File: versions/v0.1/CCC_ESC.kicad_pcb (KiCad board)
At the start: 4 copper layers, 100 x 65 mm, 160 parts, among them J1 Conn_01x04, J2 Conn_01x04, J3 Conn_01x06, J4 Conn_01x06, U1 NCP5183, U2 NCP5183, U3 NCP5183, U4 NCS20074D, U5 STM32F401CCU6_Balckpill, U6 PQDE6W-Q110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

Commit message: work in progress - some schematic updates, some minor routing
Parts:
- CX17: footprint Capacitor_SMD:C_1210_3225Metric -> Capacitor_THT:CP_Radial_D10.0mm_P5.00mm
- moved CX17 7.53 mm to (46.1, 88.4), turned to 180 degrees
- moved R1 1.91 mm to (52.9, 87.7)
- moved C31 1.42 mm to (97.7, 98.3)
- moved C5 1.30 mm to (54.7, 87.6)
- moved R5 1.10 mm to (97.5, 103.8)
- moved R10 1.10 mm to (97.5, 100.0)
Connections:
- J3 pad 1: Net-(J3-Pad1) -> Net-(RN4-Pad5)
- J3 pad 3: Net-(J3-Pad3) -> Net-(RN4-Pad7)
- RN1 pad 6: Net-(J3-Pad3) -> Net-(RN4-Pad7)
- RN1 pad 8: Net-(J3-Pad1) -> Net-(RN4-Pad5)
- RN4 pad 5: Net-(J3-Pad3) -> Net-(RN4-Pad5)
- RN4 pad 7: Net-(J3-Pad1) -> Net-(RN4-Pad7)
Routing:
- net GND: track 29.0 -> 36.3 mm, vias 213 -> 218
- net A_PHC_VSENSE: track 34.9 -> 33.3 mm
- net PHASE_C: track 13.4 -> 12.5 mm
- net PHASE_A: track 22.7 -> 21.8 mm

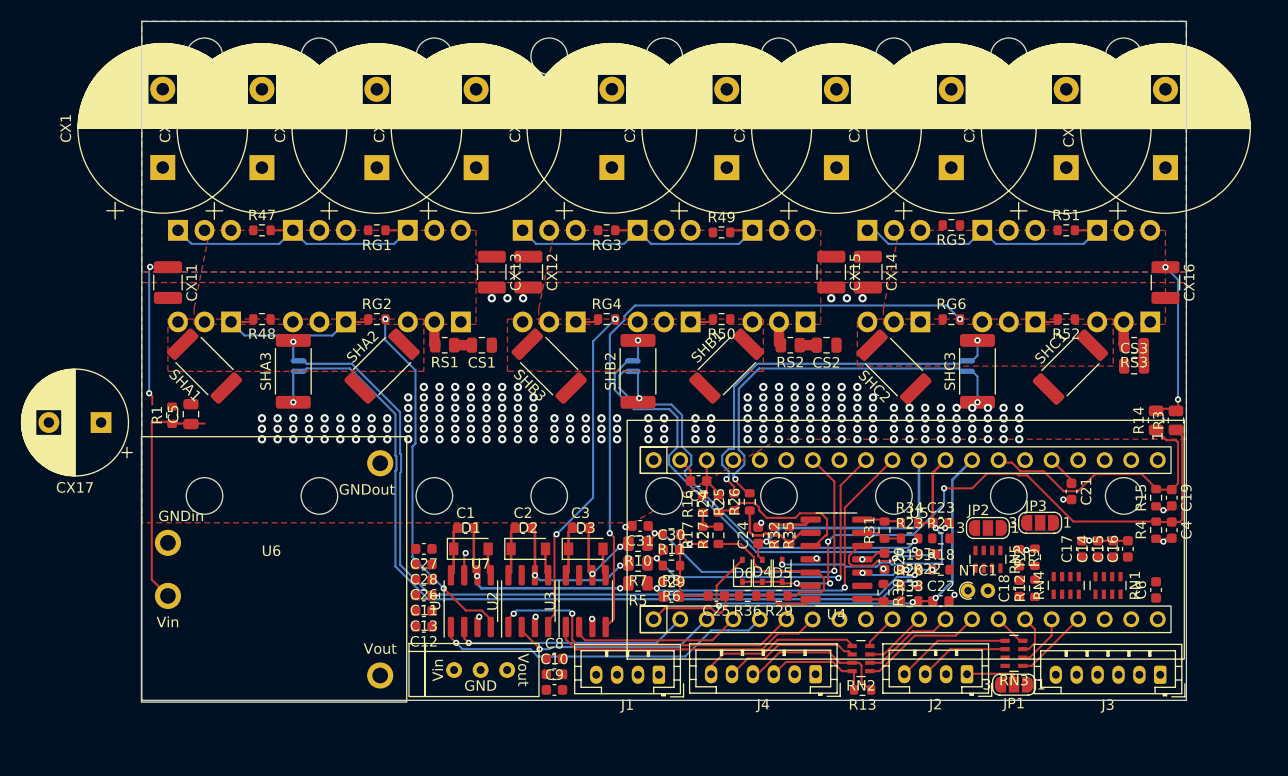
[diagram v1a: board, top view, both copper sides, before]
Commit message: added cap and JST
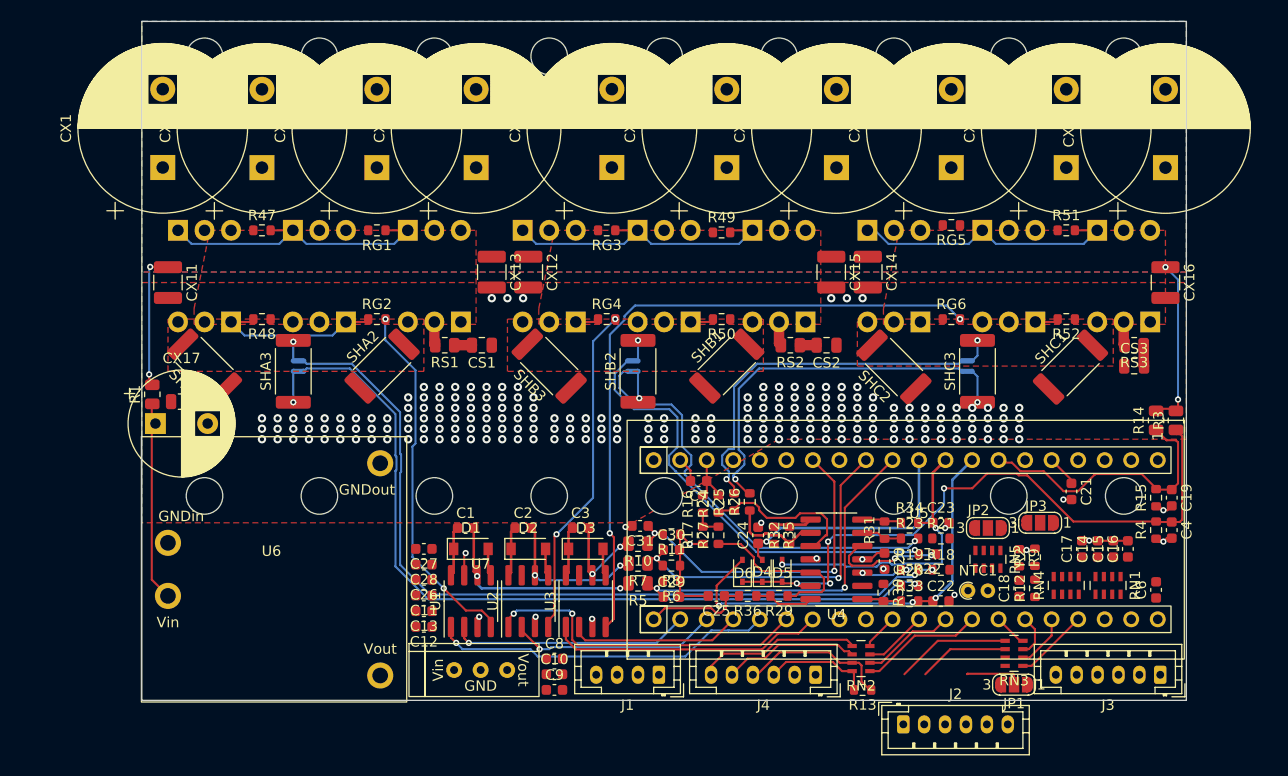
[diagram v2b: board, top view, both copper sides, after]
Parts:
- J2: value Conn_01x04 -> Conn_01x06; footprint Connector_JST:JST_PH_B4B-PH-K_1x04_P2.00mm_Vertical -> Connector_JST:JST_PH_B6B-PH-K_1x06_P2.00mm_Vertical
- R1: footprint Resistor_SMD:R_0603_1608Metric -> Resistor_SMD:R_0805_2012Metric
- moved J2 7.76 mm to (122.9, 117.3), turned to 0 degrees
- moved CX17 5.20 mm to (51.3, 88.5), turned to 0 degrees
- moved R1 2.76 mm to (51.0, 85.7)
- moved C5 1.53 mm to (53.8, 86.4), turned to 0 degrees
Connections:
- J2 pad 3: PB7 D_UART1_RX I2C1_SDA TIM4_CH2 -> PB9 DI2C1_SDA TIM4_CH4
- J2 pad 4: PB6 D_UART1_TX I2C1_SCL TIM4_CH1 -> PB8 DI2C1_SCL TIM4_CH3
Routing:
- net Net-(C5-Pad1): track 22.4 -> 18.8 mm
- net VBAT: track 31.1 -> 28.9 mm

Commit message: gate drivers PCB change and other minor stuff
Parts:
- JP1, JP2, JP3: moved to B.Cu
- moved C28 18.9 mm to (95.8, 103.8), turned to -90 degrees
- moved C27 12.3 mm to (88.8, 103.8), turned to -90 degrees
- moved J2 9.67 mm to (131.3, 112.6), turned to 180 degrees
- moved C18 7.55 mm to (137.8, 97.8), turned to 180 degrees
- moved C11 7.45 mm to (77.3, 112.4)
- moved C13 7.45 mm to (77.3, 113.9)
- moved C12 6.82 mm to (80.3, 113.9), turned to 0 degrees
- moved RN3 6.40 mm to (131.9, 104.3), turned to -90 degrees
- moved C9 6.10 mm to (83.4, 113.8), turned to 180 degrees
- moved C26 4.87 mm to (81.8, 103.8), turned to -90 degrees
- moved R12 4.58 mm to (138.2, 100.6)
- moved C10 3.36 mm to (86.4, 113.8)
- moved JP2 3.33 mm to (129.2, 95.7), turned to 0 degrees
- moved NTC1 3.21 mm to (129.3, 101.3)
- moved C1 3.15 mm to (77.8, 98.5)
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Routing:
- net V5V: track 0.00 -> 63.7 mm
- net PB6 D_UART1_TX I2C1_SCL TIM4_CH1: track 11.0 -> 0.00 mm
- net PB7 D_UART1_RX I2C1_SDA TIM4_CH2: track 8.64 -> 0.00 mm
- net Net-(RN3-Pad1): track 7.14 -> 0.00 mm
- net A_PHC_VSENSE: track 33.3 -> 26.5 mm
- net A_PHB_VSENSE: track 33.7 -> 27.1 mm
- net Vaux: track 5.51 -> 0.00 mm
- net A_PHA_VSENSE: track 35.4 -> 29.9 mm
- net Net-(RN3-Pad2): track 5.18 -> 0.00 mm
- net PHASE_A: track 21.8 -> 27.0 mm
- net GND: track 36.3 -> 31.5 mm
- net Net-(RN3-Pad3): track 4.05 -> 0.00 mm
- net PHASE_B: track 17.4 -> 21.2 mm
- net Net-(RN3-Pad4): track 3.18 -> 0.00 mm
- net LIN_A: track 22.9 -> 25.9 mm
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
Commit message: minor thing
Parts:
- moved U7 0.20 mm to (77.6, 109.6)
- moved C8 0.16 mm to (87.8, 112.3)
- moved C10 0.11 mm to (86.5, 113.9)
- moved C9 0.10 mm to (83.4, 113.9)
- moved C11 0.05 mm to (77.3, 112.3)
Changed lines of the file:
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@@
   )
   (footprint "Capacitor_SMD:C_0603_1608Metric" (layer "F.Cu")
-    (at 86.4 113.8)
+    (at 86.45 113.9)
     (descr "Capacitor SMD 0603 (1608 Metric), square (rectangular) end terminal, IPC_7351 nominal, (Body size source: IPC-SM-782 page 76, https://www.pcb-3d.com/wordpress/wp-content/uploads/ipc-sm-782a_amendment_1_and_2.pdf), generated with kicad-footprint-generator")
     (tags "capacitor")
@@
   )
   (footprint "CCC_ESC_Custom_parts:TO220_replacement_module" (layer "F.Cu")
-    (at 77.355 109.555)
+    (at 77.555 109.555)
     (property "Sheetfile" "CCC_ESC.kicad_sch")
     (property "Sheetname" "")
@@
   )
   (footprint "Capacitor_SMD:C_0603_1608Metric" (layer "F.Cu")
-    (at 87.6 112.3)
+    (at 87.75 112.35)
     (descr "Capacitor SMD 0603 (1608 Metric), square (rectangular) end terminal, IPC_7351 nominal, (Body size source: IPC-SM-782 page 76, https://www.pcb-3d.com/wordpress/wp-content/uploads/ipc-sm-782a_amendment_1_and_2.pdf), generated with kicad-footprint-generator")
     (tags "capacitor")
@@
   )
   (footprint "Capacitor_SMD:C_0603_1608Metric" (layer "F.Cu")
-    (at 77.3 112.4 180)
+    (at 77.3 112.35 180)
     (descr "Capacitor SMD 0603 (1608 Metric), square (rectangular) end terminal, IPC_7351 nominal, (Body size source: IPC-SM-782 page 76, https://www.pcb-3d.com/wordpress/wp-content/uploads/ipc-sm-782a_amendment_1_and_2.pdf), generated with kicad-footprint-generator")
     (tags "capacitor")
@@
   )
   (footprint "Capacitor_SMD:C_0603_1608Metric" (layer "F.Cu")
-    (at 83.4 113.8 180)
+    (at 83.4 113.9 180)
     (descr "Capacitor SMD 0603 (1608 Metric), square (rectangular) end terminal, IPC_7351 nominal, (Body size source: IPC-SM-782 page 76, https://www.pcb-3d.com/wordpress/wp-content/uploads/ipc-sm-782a_amendment_1_and_2.pdf), generated with kicad-footprint-generator")
     (tags "capacitor")

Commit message: minor schematic + routing optimisation
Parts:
- moved NTC1 4.00 mm to (133.3, 101.2)
- moved RN3 1.18 mm to (130.8, 104.0)
- moved RN4 1.10 mm to (137.4, 104.0)
- moved JP2 1.05 mm to (130.2, 95.8)
- moved C6 0.70 mm to (147.8, 104.4)
- moved U4 0.25 mm to (116.5, 101.2)
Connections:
- RN4 pad 5: Net-(J3-Pad1) -> Net-(J3-Pad5)
- RN4 pad 6: Net-(J3-Pad2) -> Net-(J3-Pad3)
- RN4 pad 7: Net-(J3-Pad3) -> Net-(J3-Pad2)
- RN4 pad 8: Net-(J3-Pad5) -> Net-(J3-Pad1)
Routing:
- net Vaux: track 0.00 -> 25.5 mm
- net Net-(R18-Pad1): track 7.62 -> 6.59 mm
- net GND: track 31.5 -> 30.8 mm
- net Net-(R21-Pad1): track 11.4 -> 10.8 mm

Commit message: some fancy routing
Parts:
- moved C18 24.4 mm to (113.6, 94.5), turned to -90 degrees
- moved NTC1 21.5 mm to (154.5, 98.2)
- moved R12 17.2 mm to (155.4, 100.0), turned to 180 degrees
- moved RN4 7.85 mm to (145.3, 103.9), turned to 180 degrees
- moved JP2 7.11 mm to (134.8, 101.3), turned to 180 degrees
- moved RN5 5.82 mm to (130.5, 104.3), turned to 90 degrees
- moved C17 4.92 mm to (135.2, 99.7), turned to 180 degrees
- moved R2 4.84 mm to (131.6, 101.3)
- moved R9 4.76 mm to (130.1, 101.3)
- moved RN3 3.76 mm to (134.5, 104.3)
- moved C21 2.98 mm to (139.7, 97.9), turned to 180 degrees
- moved JP3 2.31 mm to (136.2, 98.0), turned to 180 degrees
- moved C14 1.60 mm to (139.9, 100.5)
- moved C15 1.55 mm to (141.4, 100.5)
- moved C16 1.40 mm to (143.0, 100.5)
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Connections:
- RN4 pad 5: Net-(J3-Pad5) -> Net-(J3-Pad1)
- RN4 pad 6: Net-(J3-Pad3) -> Net-(J3-Pad2)
- RN4 pad 7: Net-(J3-Pad2) -> Net-(J3-Pad3)
- RN4 pad 8: Net-(J3-Pad1) -> Net-(J3-Pad5)
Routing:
- net A_THROTTLE: track 0.00 -> 17.4 mm
- net Net-(J3-Pad1): track 0.00 -> 17.3 mm
- net PB6 D_UART1_TX I2C1_SCL TIM4_CH1: track 0.00 -> 17.3 mm
- net Net-(J3-Pad5): track 0.00 -> 16.6 mm
- net PB7 D_UART1_RX I2C1_SDA TIM4_CH2: track 0.00 -> 15.9 mm
- net PB8 DI2C1_SCL TIM4_CH3: track 0.00 -> 15.2 mm
- net HALL_C: track 0.00 -> 14.3 mm
- net HALL_A: track 0.00 -> 14.0 mm
- net PB9 DI2C1_SDA TIM4_CH4: track 0.00 -> 13.6 mm
- net Net-(J3-Pad2): track 0.00 -> 12.5 mm
- net Net-(J3-Pad3): track 0.00 -> 12.1 mm
- net HALL_B: track 0.00 -> 11.7 mm, vias 0 -> 2
- net V3V3: track 6.88 -> 13.3 mm
- net Net-(R2-Pad1): track 0.00 -> 6.24 mm
- net A_PHC_VSENSE: track 26.5 -> 31.8 mm
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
